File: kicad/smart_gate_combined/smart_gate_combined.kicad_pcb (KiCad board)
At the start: 2 copper layers, 250 x 150 mm, 31 parts

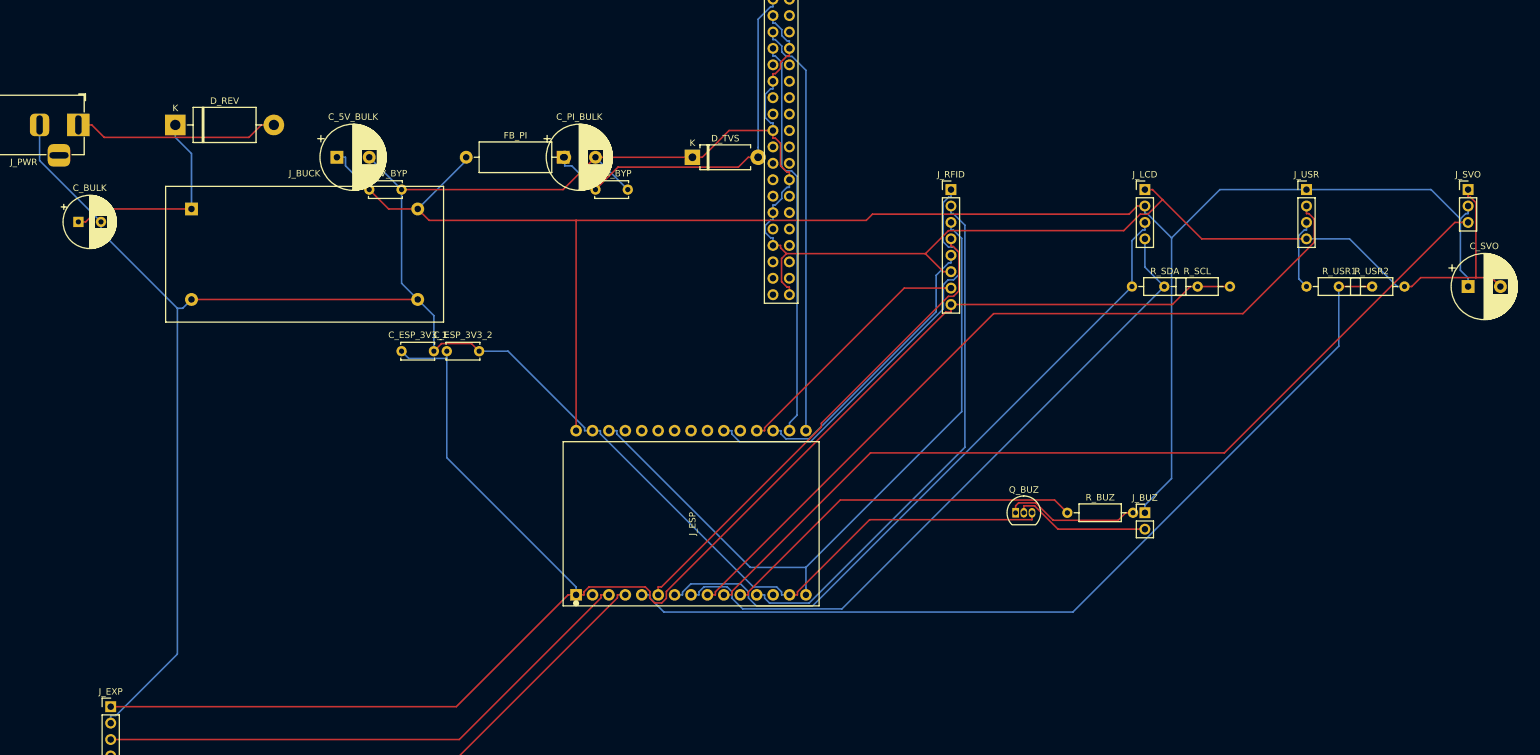
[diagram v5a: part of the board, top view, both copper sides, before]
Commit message: fix(kicad): LM2596S adjustable buck — corrected pad spacing 37x13mm
LM2596S adjustable mini buck module standard dimensions:
  - PCB body: 43 x 21 mm (unchanged in silkscreen outline)
  - Pad spacing horizontal IN-to-OUT: 37 mm (was 35mm, off by 2mm)
  - Pad spacing vertical V+ to GND: 13 mm (was 14mm, off by 1mm)
  - Drill: 1.2mm (was 1.0mm), pad: 2.2mm (was 2.0mm) for ~0.1mm headroom

User does not have caliper to verify exact module dimensions — these are
the most-cited values from cheap Chinese LM2596S modules common in Vietnam.
If actual module's pads don't align, edit (at X Y) in the 4 pad lines of
footprints.pretty/LM2596_Mini_Buck.kicad_mod and re-run pipeline.

Co-Authored-By: Claude Opus 4.7 <noreply@anthropic.com>
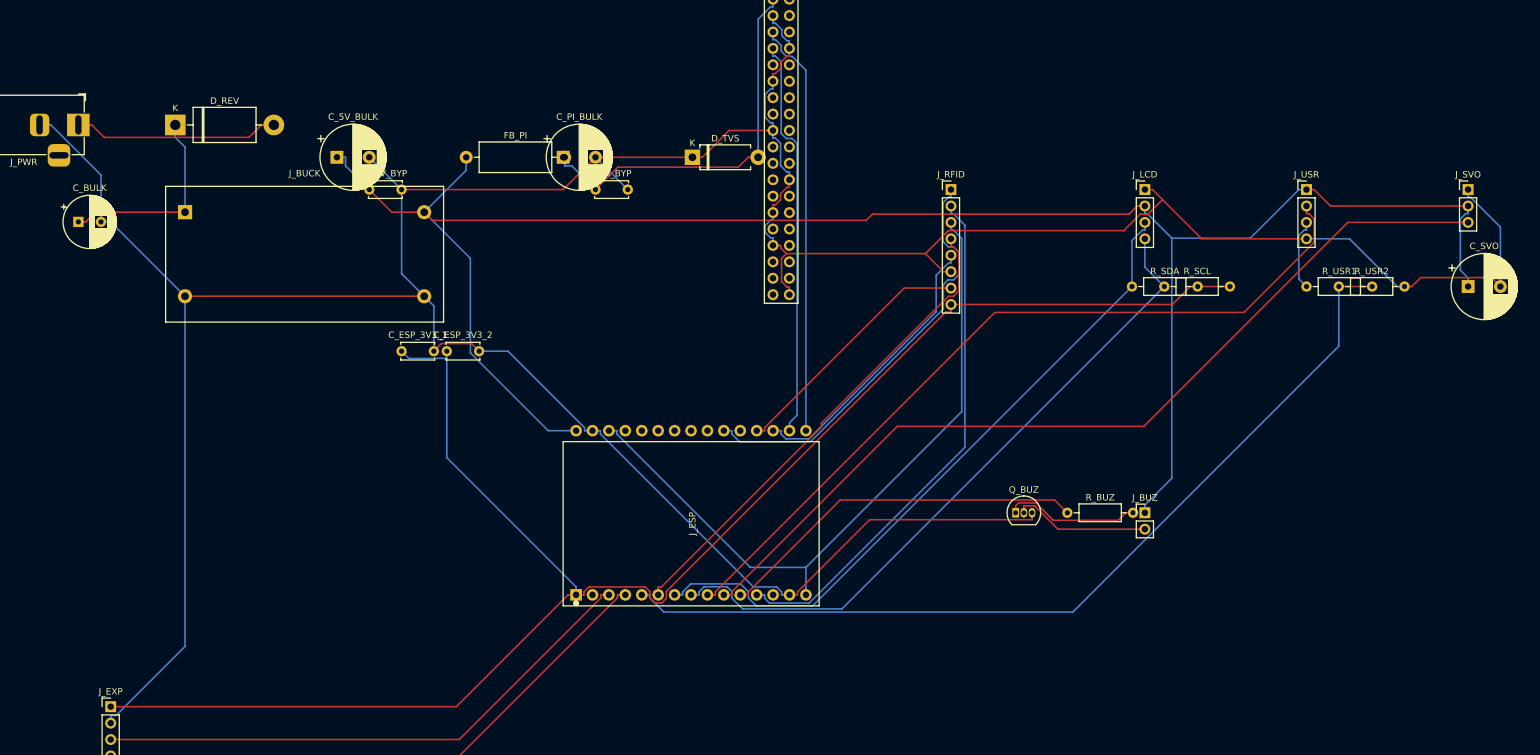
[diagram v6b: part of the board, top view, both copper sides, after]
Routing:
- net +5V: track 288.8 -> 302.8 mm
- net GND: track 560.4 -> 565.5 mm
- net +12V: track 32.4 -> 31.2 mm

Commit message: feat(kicad): force B.Cu signal routing + flip GND pour to F.Cu
User wants components on opposite side from wires. For THT prototype:
- Components remain on F.Cu (top, body + silkscreen)
- Wires route on B.Cu (bottom) only — clean separation
- GND copper pour moves to F.Cu (fills around components on top)

Implementation:
- autoroute.py post-processes DSN to set F.Cu type=power (not signal)
  -> FreeRouting routes only on B.Cu
- add_gnd_pour.py now creates zone on F.Cu (was B.Cu)
- Removed FB_PI ferrite bead — Pi GPIO 5V now ties directly to +5V net

Result: 282 B.Cu tracks (88%%) vs 37 F.Cu tracks (12%% are unavoidable
pad escape stubs). 7 vias for B->F transitions.

Co-Authored-By: Claude Opus 4.7 <noreply@anthropic.com>
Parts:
- moved J_EXP 234.7 mm to (251.5, 35.6), turned to 90 degrees
- moved J_ESP 156.5 mm to (218.4, 45.7), turned to 0 degrees
- moved H4 136.0 mm to (269.2, 132.1)
- moved R_SDA 120.9 mm to (246.4, 48.3), turned to -90 degrees
- moved H3 116.3 mm to (77.3, 132.1)
- moved H2 112.2 mm to (269.0, 22.5)
- moved C_BULK 108.8 mm to (76.2, 53.3)
- moved J_PWR 107.2 mm to (84.7, 37.1)
- moved J_RFID 103.4 mm to (259.1, 47.0)
- moved J_BUCK 99.3 mm to (86.4, 83.8), turned to -90 degrees
- moved R_USR2 99.2 mm to (246.4, 88.9), turned to 90 degrees
- moved Q_BUZ 98.8 mm to (236.2, 104.1), turned to 180 degrees
- moved R_SCL 98.4 mm to (246.4, 73.7), turned to 90 degrees
- moved D_REV 93.8 mm to (94.0, 53.3), turned to 90 degrees
- moved J_BUZ 91.7 mm to (236.2, 119.4), turned to -90 degrees
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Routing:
- net RC522_MOSI: track 108.0 -> 28.5 mm
- net HCSR_ECHO_3V3: track 140.6 -> 67.2 mm
- net SERVO_PWM: track 139.3 -> 71.5 mm
- net HCSR_TRIG: track 123.1 -> 64.4 mm
- net +5V: track 302.8 -> 252.2 mm
- net I2C_SDA: track 105.1 -> 68.7 mm
- net +3V3: track 257.8 -> 228.3 mm, vias 0 -> 1
- net IO36: track 86.6 -> 64.0 mm
- net N$1: track 31.8 -> 9.64 mm
- net RC522_CS: track 65.6 -> 43.9 mm
- net GND: track 565.5 -> 587.0 mm, vias 0 -> 3
- net RC522_MISO: track 75.8 -> 54.9 mm
- net IO39: track 90.2 -> 70.2 mm
- net I2C_SCL: track 105.3 -> 87.5 mm
- net HCSR_ECHO_5V: track 11.1 -> 21.1 mm
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- added copper zone on F.Cu, net GND
- removed copper zone on B.Cu, net GND
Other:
- board size 250 x 150 mm -> 201.7 x 119.6 mm
